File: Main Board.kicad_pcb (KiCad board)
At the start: 2 copper layers, 268 parts, among them J1 Motor Y, J10 CA58SUB-B, J11 PC6 EPSON MAINBOARD, J12 WASTE INK, J13 LED 1, J14 LED 2, J15 Y AXIS, J16 Z AXIS, J17 Power Input, J18 TABLE SENSOR, J19 PHOTO SENSOR EMITER, J2 Motor Z, J20 PHOTO SENSOR RECEIVER, J21 EMERGENCY, J22 EPSON POWER IN, J23 EPSON BOARD POWER, J24 Display, J25 SPI Interface, J26 I2C Interface, J27 LED3, J28 LED4, J29 Key 3, J3 USB_B, J30 Key 4, J31 Key 1, J32 Key 2, J4 SWD, J5 DEBUG, J6 LIMIT Z UP, J7 LIMIT Z DOWN, J8 LIMIT Y BACK, J9 LIMIT Y FRONT, K1 S13-24V-2C, Q1 BC817, Q2 BC817, Q3 BC817, Q4 YJS9435A, Q5 BC817, Q6 BC817, Q7 BC817, Q8 BC817, Q9 BC817, U1 TMC2209-LA, U10 SHTC3, U2 TMC2209-LA, U3 STM32F401VETx, U4 USBUF02W6, U5 74HC245, U6 A4403, U7 MCP16301, U8 74HC2G32, U9 74HC245, Y1 8MHz

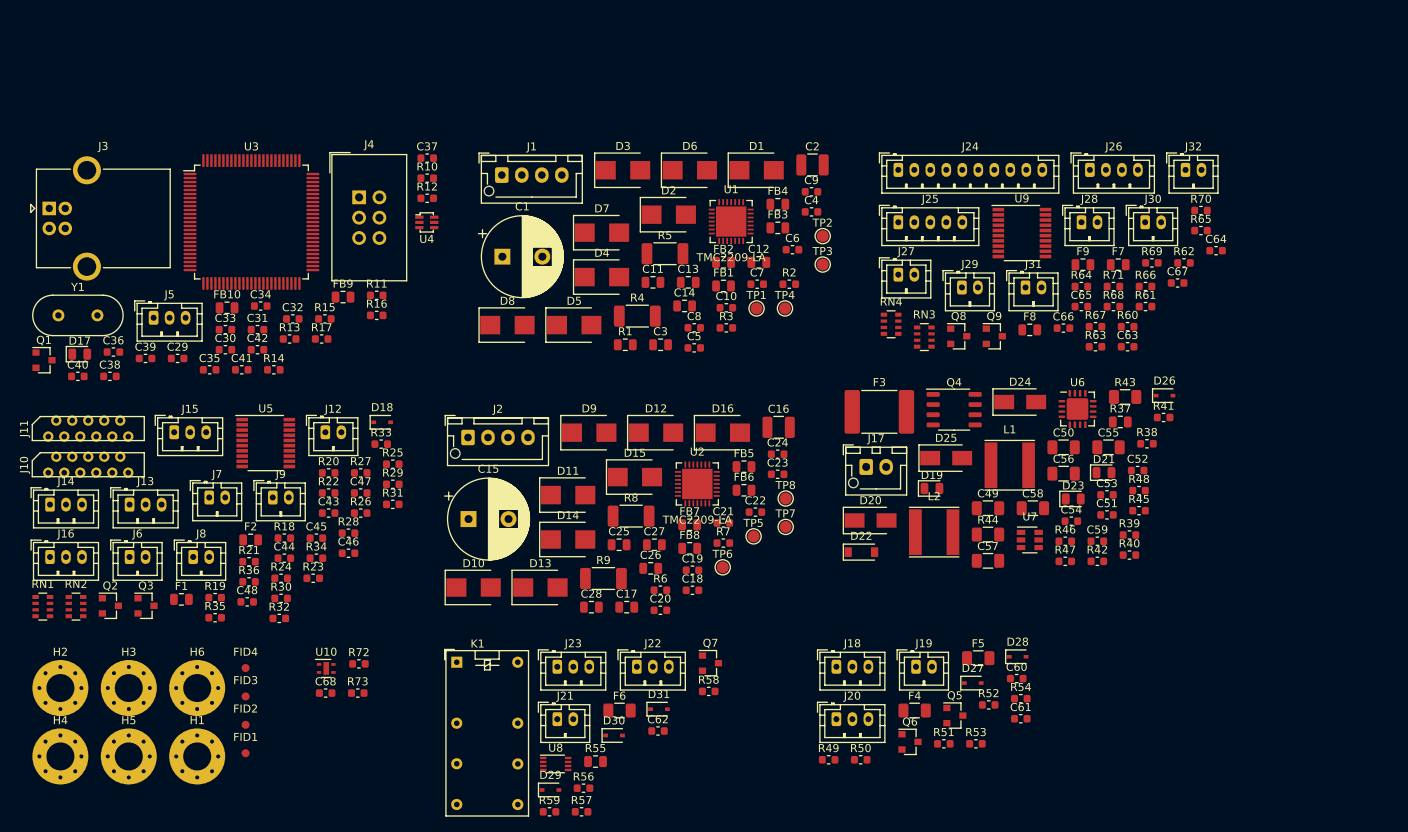
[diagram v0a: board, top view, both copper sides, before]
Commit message: Added 12V regulator, aditional input, outputs, improved inputs ESD
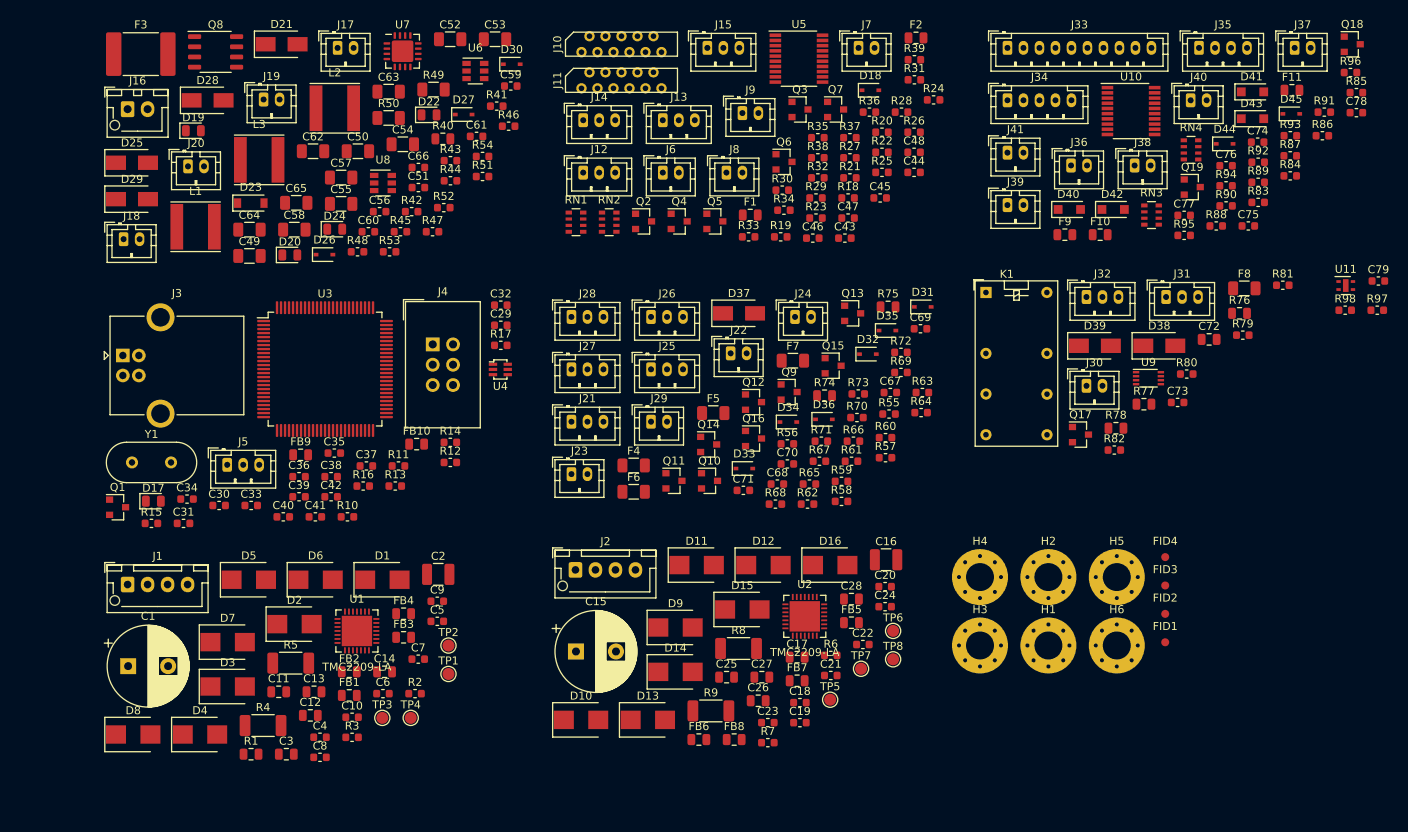
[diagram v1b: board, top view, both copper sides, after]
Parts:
- added C69: 1nF, Capacitor_SMD:C_0603_1608Metric, F.Cu at (137.9, -56.3)
- added C70: 1nF, Capacitor_SMD:C_0603_1608Metric, F.Cu at (121.2, -39.4)
- added C71: 1nF, Capacitor_SMD:C_0603_1608Metric, F.Cu at (115.7, -36.1)
- added C72: NI, Capacitor_SMD:C_0805_2012Metric, F.Cu at (174.0, -54.9)
- added C73: 1nF, Capacitor_SMD:C_0603_1608Metric, F.Cu at (170.0, -47.1)
- added C74: 0.1uF, Capacitor_SMD:C_0603_1608Metric, F.Cu at (180.0, -79.6)
- added C75: 1nF, Capacitor_SMD:C_0603_1608Metric, F.Cu at (178.9, -69.1)
- added C76: 1nF, Capacitor_SMD:C_0603_1608Metric, F.Cu at (176.1, -76.6)
- added C77: 1nF, Capacitor_SMD:C_0603_1608Metric, F.Cu at (170.8, -70.4)
- added C78: 1nF, Capacitor_SMD:C_0603_1608Metric, F.Cu at (192.4, -83.3)
- added C79: 0.1uF, Capacitor_SMD:C_0603_1608Metric, F.Cu at (195.1, -62.2)
- added D32: 1N4448WS-7-F, Diode_SMD:D_SOD-323, F.Cu at (131.3, -53.1)
- added D33: 1N4448WS-7-F, Diode_SMD:D_SOD-323, F.Cu at (115.9, -38.8)
- added D34: SD05C.TCT, Diode_SMD:D_SOD-323, F.Cu at (121.4, -44.6)
- added D35: SD05C.TCT, Diode_SMD:D_SOD-323, F.Cu at (133.8, -56.0)
- added D36: SD05C.TCT, Diode_SMD:D_SOD-323, F.Cu at (125.8, -44.9)
- added D37: B130-13-F, Diode_SMD:D_SMA, F.Cu at (115.2, -58.2)
- added D38: B130-13-F, Diode_SMD:D_SMA, F.Cu at (167.7, -54.1)
- added D39: B130-13-F, Diode_SMD:D_SMA, F.Cu at (159.7, -54.1)
- added D40: SKL32, Diode_SMD:D_SOD-123F, F.Cu at (156.5, -71.2)
- added D41: SKL32, Diode_SMD:D_SOD-123F, F.Cu at (179.4, -85.9)
- added D42: SKL32, Diode_SMD:D_SOD-123F, F.Cu at (162.0, -71.2)
- added D43: SKL32, Diode_SMD:D_SOD-123F, F.Cu at (179.4, -82.5)
- added D44: SD05C.TCT, Diode_SMD:D_SOD-323, F.Cu at (175.9, -79.4)
- added D45: SD05C.TCT, Diode_SMD:D_SOD-323, F.Cu at (184.2, -83.1)
- added F10: SR050, Fuse:Fuse_0805_2012Metric, F.Cu at (160.3, -68.0)
- added F11: SR010, Fuse:Fuse_0805_2012Metric, F.Cu at (184.3, -86.1)
- added J33: Display, Connector_JST:JST_PH_B10B-PH-K_1x10_P2.00mm_Vertical, F.Cu at (148.8, -91.4)
- added J34: SPI Interface, Connector_JST:JST_PH_B5B-PH-K_1x05_P2.00mm_Vertical, F.Cu at (148.8, -84.8)
- added J35: I2C Interface, Connector_JST:JST_PH_B4B-PH-K_1x04_P2.00mm_Vertical, F.Cu at (172.7, -91.4)
- added J36: LED4, Connector_JST:JST_PH_B2B-PH-K_1x02_P2.00mm_Vertical, F.Cu at (156.7, -76.7)
- added J37: LED3, Connector_JST:JST_PH_B2B-PH-K_1x02_P2.00mm_Vertical, F.Cu at (184.7, -91.4)
- added J38: Key 3, Connector_JST:JST_PH_B2B-PH-K_1x02_P2.00mm_Vertical, F.Cu at (164.7, -76.7)
- added J39: Key 4, Connector_JST:JST_PH_B2B-PH-K_1x02_P2.00mm_Vertical, F.Cu at (148.8, -71.7)
- added J40: Key 1, Connector_JST:JST_PH_B2B-PH-K_1x02_P2.00mm_Vertical, F.Cu at (171.7, -84.8)
- added J41: Key 2, Connector_JST:JST_PH_B2B-PH-K_1x02_P2.00mm_Vertical, F.Cu at (148.8, -78.3)
- added L3: DJNR6045-6R8, footprints:L_6.2x6.2_H4.5, F.Cu at (55.2, -77.4)
- added Q10: 2N7002K, Package_TO_SOT_SMD:SOT-23, F.Cu at (111.5, -37.3)
- added Q11: BC817, Package_TO_SOT_SMD:SOT-23, F.Cu at (107.1, -37.3)
- added Q12: BC817, Package_TO_SOT_SMD:SOT-23, F.Cu at (117.0, -47.1)
- added Q13: BC817, Package_TO_SOT_SMD:SOT-23, F.Cu at (129.4, -58.2)
- added Q14: 2N7002K, Package_TO_SOT_SMD:SOT-23, F.Cu at (111.4, -41.8)
- added Q15: 2N7002K, Package_TO_SOT_SMD:SOT-23, F.Cu at (127.0, -51.6)
- added Q16: 2N7002K, Package_TO_SOT_SMD:SOT-23, F.Cu at (117.0, -42.5)
- added Q17: BC817, Package_TO_SOT_SMD:SOT-23, F.Cu at (157.9, -43.0)
- added Q18: 2N7002K, Package_TO_SOT_SMD:SOT-23, F.Cu at (191.9, -91.8)
- added Q19: 2N7002K, Package_TO_SOT_SMD:SOT-23, F.Cu at (171.9, -74.0)
- added R74: NI, Resistor_SMD:R_0805_2012Metric, F.Cu at (125.9, -47.9)
- added R75: NI, Resistor_SMD:R_0805_2012Metric, F.Cu at (133.8, -59.0)
- added R76: 0Ω, Resistor_SMD:R_0805_2012Metric, F.Cu at (177.8, -58.2)
- added R77: NI, Resistor_SMD:R_0805_2012Metric, F.Cu at (165.8, -46.8)
- added R78: NI, Resistor_SMD:R_0805_2012Metric, F.Cu at (162.3, -43.8)
- added R79: 100kΩ, Resistor_SMD:R_0603_1608Metric, F.Cu at (178.2, -55.5)
- added R80: 1kΩ, Resistor_SMD:R_0603_1608Metric, F.Cu at (171.2, -50.6)
- added R81: 100kΩ, Resistor_SMD:R_0603_1608Metric, F.Cu at (183.2, -61.7)
- added R82: 100kΩ, Resistor_SMD:R_0603_1608Metric, F.Cu at (162.1, -41.1)
- added R83: 20Ω, Resistor_SMD:R_0603_1608Metric, F.Cu at (180.1, -72.1)
- added R84: 20Ω, Resistor_SMD:R_0603_1608Metric, F.Cu at (184.1, -75.4)
- added R85: 100Ω, Resistor_SMD:R_0603_1608Metric, F.Cu at (192.4, -85.8)
- added R86: 100Ω, Resistor_SMD:R_0603_1608Metric, F.Cu at (188.1, -80.4)
- added R87: 330Ω, Resistor_SMD:R_0603_1608Metric, F.Cu at (184.1, -77.9)
- added R88: 330Ω, Resistor_SMD:R_0603_1608Metric, F.Cu at (174.9, -69.1)
- added R89: 4.7kΩ, Resistor_SMD:R_0603_1608Metric, F.Cu at (180.1, -74.6)
- added R90: 4.7kΩ, Resistor_SMD:R_0603_1608Metric, F.Cu at (176.1, -71.6)
- added R91: 4.7kΩ, Resistor_SMD:R_0603_1608Metric, F.Cu at (188.4, -83.3)
- added R92: 4.7kΩ, Resistor_SMD:R_0603_1608Metric, F.Cu at (180.1, -77.1)
- added R93: 1kΩ, Resistor_SMD:R_0603_1608Metric, F.Cu at (184.1, -80.4)
- added R94: 1kΩ, Resistor_SMD:R_0603_1608Metric, F.Cu at (176.1, -74.1)
- added R95: 1kΩ, Resistor_SMD:R_0603_1608Metric, F.Cu at (170.8, -67.9)
- added R96: 1kΩ, Resistor_SMD:R_0603_1608Metric, F.Cu at (191.6, -88.3)
- added R97: 2.2kΩ, Resistor_SMD:R_0603_1608Metric, F.Cu at (195.0, -58.6)
- added R98: 2.2kΩ, Resistor_SMD:R_0603_1608Metric, F.Cu at (191.0, -58.6)
- added U11: SHTC3, footprints:DFN-4-1EP_2x2mm_P1mm_EP0.7x1.6mm, F.Cu at (191.0, -61.7)
- C47, C61: value 1nF -> 0.1uF
- C48, C68: value 0.1uF -> 1nF
- C51: value 47nF -> 0.1uF
- C52: value 22nF -> 2.2uF; footprint Capacitor_SMD:C_0603_1608Metric -> Capacitor_SMD:C_1206_3216Metric
- C53: value 1nF -> 2.2uF; footprint Capacitor_SMD:C_0603_1608Metric -> Capacitor_SMD:C_1206_3216Metric
- C54: value 0.1uF -> 2.2uF; footprint Capacitor_SMD:C_0603_1608Metric -> Capacitor_SMD:C_1206_3216Metric
- C55: value 10uF -> 2.2uF
- C56: value 10uF -> 47nF; footprint Capacitor_SMD:C_1206_3216Metric -> Capacitor_SMD:C_0603_1608Metric
- C59: value 10nF -> 22nF
- C62, C64, C65: value 1nF -> 10uF; footprint Capacitor_SMD:C_0603_1608Metric -> Capacitor_SMD:C_1206_3216Metric
- C63: value 0.1uF -> 10uF; footprint Capacitor_SMD:C_0603_1608Metric -> Capacitor_SMD:C_1206_3216Metric
- C66: value 1nF -> 10nF
- D18: value 1N4448WS-7-F -> SD05C.TCT
- D20: value P4SMA30CA -> OF-SMD2012G-1; footprint Diode_SMD:D_SMA -> Diode_SMD:D_0805_2012Metric
- D21: value OF-SMD2012G-1 -> P4SMA30CA; footprint Diode_SMD:D_0805_2012Metric -> Diode_SMD:D_SMA
- D22: value MMSZ5240B-7-F -> OF-SMD2012G-1; footprint Diode_SMD:D_SOD-123 -> Diode_SMD:D_0805_2012Metric
- D23: value OF-SMD2012G-1 -> MMSZ5240B-7-F; footprint Diode_SMD:D_0805_2012Metric -> Diode_SMD:D_SOD-123
- D24: value B140-13-F -> OF-SMD2012G-1; footprint Diode_SMD:D_SMA -> Diode_SMD:D_0805_2012Metric
- D25: value SK35SMA -> B140-13-F
- D27: value 1N4448WS-7-F -> MMSZ5236BS-7-F
- D28: value 1N4448WS-7-F -> B140-13-F; footprint Diode_SMD:D_SOD-323 -> Diode_SMD:D_SMA
- D29: value 1N4448WS-7-F -> SK35SMA; footprint Diode_SMD:D_SOD-323 -> Diode_SMD:D_SMA
- F7: value SR010 -> Polyfuse; footprint Fuse:Fuse_0805_2012Metric -> Fuse:Fuse_1206_3216Metric
- F8: value SR050 -> SN010-60; footprint Fuse:Fuse_0805_2012Metric -> Fuse:Fuse_1206_3216Metric
- J12: value WASTE INK -> Y AXIS; footprint Connector_JST:JST_PH_B2B-PH-K_1x02_P2.00mm_Vertical -> Connector_JST:JST_PH_B3B-PH-K_1x03_P2.00mm_Vertical
- J13: value LED 1 -> Z AXIS
- J14: value LED 2 -> LED 1
- J15: value Y AXIS -> LED 2
- J16: value Z AXIS -> Power Input; footprint Connector_JST:JST_PH_B3B-PH-K_1x03_P2.00mm_Vertical -> Connector_JST:JST_XH_B2B-XH-AM_1x02_P2.50mm_Vertical
- J17: value Power Input -> VS; footprint Connector_JST:JST_XH_B2B-XH-AM_1x02_P2.50mm_Vertical -> Connector_JST:JST_PH_B2B-PH-K_1x02_P2.00mm_Vertical
- J18: value TABLE SENSOR -> 12V; footprint Connector_JST:JST_PH_B3B-PH-K_1x03_P2.00mm_Vertical -> Connector_JST:JST_PH_B2B-PH-K_1x02_P2.00mm_Vertical
- J19: value PHOTO SENSOR EMITER -> 5V
- J20: value PHOTO SENSOR RECEIVER -> 3.3V; footprint Connector_JST:JST_PH_B3B-PH-K_1x03_P2.00mm_Vertical -> Connector_JST:JST_PH_B2B-PH-K_1x02_P2.00mm_Vertical
- J21: value EMERGENCY -> TABLE SENSOR; footprint Connector_JST:JST_PH_B2B-PH-K_1x02_P2.00mm_Vertical -> Connector_JST:JST_PH_B3B-PH-K_1x03_P2.00mm_Vertical
- J22: value EPSON POWER IN -> INPUT1; footprint Connector_JST:JST_PH_B3B-PH-K_1x03_P2.00mm_Vertical -> Connector_JST:JST_PH_B2B-PH-K_1x02_P2.00mm_Vertical
- J23: value EPSON BOARD POWER -> INPUT2; footprint Connector_JST:JST_PH_B3B-PH-K_1x03_P2.00mm_Vertical -> Connector_JST:JST_PH_B2B-PH-K_1x02_P2.00mm_Vertical
- J24: value Display -> PHOTO SENSOR EMITER; footprint Connector_JST:JST_PH_B10B-PH-K_1x10_P2.00mm_Vertical -> Connector_JST:JST_PH_B2B-PH-K_1x02_P2.00mm_Vertical
- J25: value SPI Interface -> PHOTO SENSOR RECEIVER; footprint Connector_JST:JST_PH_B5B-PH-K_1x05_P2.00mm_Vertical -> Connector_JST:JST_PH_B3B-PH-K_1x03_P2.00mm_Vertical
- J26: value I2C Interface -> INPUT3; footprint Connector_JST:JST_PH_B4B-PH-K_1x04_P2.00mm_Vertical -> Connector_JST:JST_PH_B3B-PH-K_1x03_P2.00mm_Vertical
- J27: value LED3 -> OUT1; footprint Connector_JST:JST_PH_B2B-PH-K_1x02_P2.00mm_Vertical -> Connector_JST:JST_PH_B3B-PH-K_1x03_P2.00mm_Vertical
- J28: value LED4 -> OUT2; footprint Connector_JST:JST_PH_B2B-PH-K_1x02_P2.00mm_Vertical -> Connector_JST:JST_PH_B3B-PH-K_1x03_P2.00mm_Vertical
- J29: value Key 3 -> RELAY
- J30: value Key 4 -> EMERGENCY
- J31: value Key 1 -> EPSON POWER IN; footprint Connector_JST:JST_PH_B2B-PH-K_1x02_P2.00mm_Vertical -> Connector_JST:JST_PH_B3B-PH-K_1x03_P2.00mm_Vertical
- J32: value Key 2 -> EPSON BOARD POWER; footprint Connector_JST:JST_PH_B2B-PH-K_1x02_P2.00mm_Vertical -> Connector_JST:JST_PH_B3B-PH-K_1x03_P2.00mm_Vertical
- J6: value LIMIT Z UP -> LIMIT Y BACK
- J7: value LIMIT Z DOWN -> LIMIT Y FRONT
- J8: value LIMIT Y BACK -> LIMIT Z UP
- J9: value LIMIT Y FRONT -> LIMIT Z DOWN
- L1: value DJNR6045-150 -> DJNR6045-680
- L2: value DJNR6045-6R8 -> DJNR6045-150
- Q2, Q3, Q5, Q6, Q7, Q9: value BC817 -> 2N7002K
- Q4: value YJS9435A -> 2N7002K; footprint Package_SO:SOP-8_3.9x4.9mm_P1.27mm -> Package_TO_SOT_SMD:SOT-23
- Q8: value BC817 -> YJS9435A; footprint Package_TO_SOT_SMD:SOT-23 -> Package_SO:SOP-8_3.9x4.9mm_P1.27mm
- R22, R23, R24, R25, R30, R71: value 1kΩ -> 100Ω
- R26, R27: value 0Ω -> 47kΩ
- R28: value NI -> 47kΩ
- R29, R70: value 1kΩ -> 47kΩ
- R31: value 4.7kΩ -> 1kΩ
- R32: value 1kΩ -> 0Ω
- R33: value 4.7kΩ -> 0Ω
- R34: value 10kΩ -> NI
- R35, R60, R61: value 4.7kΩ -> 100Ω
- R36, R69: value 1kΩ -> 100kΩ
- R37: value 10kΩ -> 47kΩ; footprint Resistor_SMD:R_0805_2012Metric -> Resistor_SMD:R_0603_1608Metric
- R38: value 330Ω -> 1kΩ
- R39: value 100kΩ -> 1kΩ
- R40: value 1kΩ -> 10kΩ; footprint Resistor_SMD:R_0603_1608Metric -> Resistor_SMD:R_0805_2012Metric
- R41: value 100kΩ -> 330Ω
- R42: value 47Ω -> 1kΩ
- R43: value 100mΩ -> 100kΩ; footprint Resistor_SMD:R_1206_3216Metric -> Resistor_SMD:R_0603_1608Metric
- R44: value 100mΩ -> 2.7kΩ; footprint Resistor_SMD:R_1206_3216Metric -> Resistor_SMD:R_0603_1608Metric
- R45: value 31.2kΩ -> 140kΩ
- R47: value 3.92kΩ -> 100kΩ
- R48: value 750Ω -> 47Ω
- R49, R50: value 10kΩ -> 100mΩ; footprint Resistor_SMD:R_0603_1608Metric -> Resistor_SMD:R_1206_3216Metric
- R51: value 33kΩ -> 31.2kΩ
- R52: value 33kΩ -> 10kΩ
- R53: value 10kΩ -> 3.92kΩ
- R54: value 10kΩ -> 750Ω
- R55: value 1kΩ -> 10kΩ; footprint Resistor_SMD:R_0805_2012Metric -> Resistor_SMD:R_0603_1608Metric
- R56: value 33kΩ -> 4.7kΩ
- R57: value 1kΩ -> 4.7kΩ
- R58: value 100kΩ -> 10kΩ
- R62: value 330Ω -> 100kΩ
- R63: value 330Ω -> 47kΩ
- R64, R65, R66: value 4.7kΩ -> 47kΩ
- R67: value 4.7kΩ -> 10kΩ
- R68: value 1kΩ -> NI
- R72, R73: value 2.2kΩ -> 100Ω
- U10: value SHTC3 -> 74HC245; footprint footprints:DFN-4-1EP_2x2mm_P1mm_EP0.7x1.6mm -> Package_SO:TSSOP-20_4.4x6.5mm_P0.65mm
- U6: value A4403 -> MCP16301; footprint Package_DFN_QFN:QFN-16-1EP_4x4mm_P0.65mm_EP2.7x2.7mm -> Package_TO_SOT_SMD:SOT-23-6
- U7: value MCP16301 -> A4403; footprint Package_TO_SOT_SMD:SOT-23-6 -> Package_DFN_QFN:QFN-16-1EP_4x4mm_P0.65mm_EP2.7x2.7mm
- U8: value 74HC2G32 -> MCP16301; footprint Package_SO:VSSOP-8_2.3x2mm_P0.5mm -> Package_TO_SOT_SMD:SOT-23-6
- U9: value 74HC245 -> 74HC2G32; footprint Package_SO:TSSOP-20_4.4x6.5mm_P0.65mm -> Package_SO:VSSOP-8_2.3x2mm_P0.5mm
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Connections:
- net Net-(J3-Pad2) renamed /Microcontroller/D-
- net Net-(J3-Pad3) renamed /Microcontroller/D+
- C43 pad 1: LIMIT_Z_UP -> LIMIT_Y_BACK
- C44 pad 1: LIMIT_Z_DOWN -> LIMIT_Y_FRONT
- C45 pad 1: LIMIT_Y_BACK -> LIMIT_Z_UP
- C46 pad 1: LIMIT_Y_FRONT -> LIMIT_Z_DOWN
- C47 pad 1: WASTE_INK -> +5V
- C48 pad 1: +5V -> PRINTER_POWER_DETECT
- C51 pad 1: GND -> Net-(C51-Pad1)
- C52 pad 1: Net-(C52-Pad1) -> VS
- C52 pad 2: Net-(C52-Pad2) -> GND
- C53 pad 1: Net-(C53-Pad1) -> VS
- C54 pad 1: Net-(C54-Pad1) -> VS
- C54 pad 2: Net-(C54-Pad2) -> GND
- C55 pad 1: +5V -> VS
- C56 pad 1: +3V3 -> GND
- C56 pad 2: GND -> Net-(C56-Pad2)
- C57 pad 1: +5V -> +12V
- C58 pad 1: +3V3 -> +12V
- C59 pad 1: +5V -> Net-(C59-Pad1)
- C60 pad 1: TABLE_SENSOR -> Net-(C60-Pad1)
- C61 pad 1: PHOTO_SENSOR -> Net-(C61-Pad1)
- C61 pad 2: GND -> Net-(C61-Pad2)
- C62 pad 1: EMERGENCY -> +5V
- C63 pad 1: +5V -> +3V3
- C64 pad 1: KEY_3 -> +5V
- C65 pad 1: KEY_4 -> +3V3
- C66 pad 1: KEY_1 -> +5V
- C66 pad 2: GND -> Net-(C66-Pad2)
- C67 pad 1: KEY_2 -> INPUT1
- C68 pad 1: +3V3 -> INPUT2
- D18 pad 1: Net-(D18-Pad1) -> /Sockets/OPE
- D22 pad 1: VS -> GND
- D23 pad 1: GND -> VS
- D24 pad 1: Net-(C54-Pad2) -> GND
- D24 pad 2: GND -> Net-(D24-Pad2)
- D25 pad 1: Net-(C52-Pad2) -> Net-(C51-Pad2)
- D25 pad 2: Net-(D25-Pad2) -> GND
- D26 pad 1: Net-(C54-Pad1) -> Net-(C51-Pad1)
- D26 pad 2: +3V3 -> Net-(D26-Pad2)
- D27 pad 1: Net-(D27-Pad1) -> +12V
- D27 pad 2: GND -> Net-(D26-Pad2)
- D28 pad 1: Net-(D28-Pad1) -> Net-(C61-Pad2)
- D29 pad 1: Net-(D29-Pad1) -> Net-(C59-Pad2)
- D29 pad 2: GND -> Net-(D29-Pad2)
- D30 pad 1: VS -> Net-(C61-Pad1)
- D30 pad 2: Net-(D30-Pad2) -> +3V3
- D31 pad 1: Net-(D30-Pad2) -> Net-(D31-Pad1)
- F3 pad 1: Net-(D20-Pad2) -> Net-(D21-Pad2)
- F6 pad 1: Net-(F6-Pad1) -> VS
- F6 pad 2: VS -> Net-(F6-Pad2)
- F7 pad 1: +5V -> Net-(D37-Pad1)
- F7 pad 2: Net-(F7-Pad2) -> +12V
- F8 pad 1: +5V -> Net-(F8-Pad1)
- F8 pad 2: Net-(F8-Pad2) -> VS
- F9 pad 1: +3V3 -> +5V
- J12 pad 1: Net-(J12-Pad1) -> /Sockets/YSTEP
- J13 pad 1: Net-(F1-Pad2) -> /Sockets/ZSTEP
- J13 pad 2: /Sockets/LED1_CNT -> GND
- J13 pad 3: GND -> /Sockets/ZDIR
- J14 pad 1: Net-(F2-Pad2) -> Net-(F1-Pad2)
- J14 pad 2: /Sockets/LED2_CNT -> /Sockets/LED1_CNT
- J15 pad 1: /Sockets/YSTEP -> Net-(F2-Pad2)
- J15 pad 2: GND -> /Sockets/LED2_CNT
- J15 pad 3: /Sockets/YDIR -> GND
- J16 pad 1: /Sockets/ZSTEP -> Net-(F3-Pad2)
- J17 pad 1: Net-(F3-Pad2) -> VS
- J18 pad 1: Net-(F4-Pad2) -> +12V
- J18 pad 2: Net-(J18-Pad2) -> GND
- J19 pad 1: Net-(F5-Pad2) -> +5V
- J20 pad 1: Net-(F5-Pad2) -> +3V3
- J20 pad 2: Net-(J20-Pad2) -> GND
- J21 pad 1: Net-(F6-Pad1) -> Net-(F4-Pad2)
- J21 pad 2: Net-(D29-Pad1) -> Net-(J21-Pad2)
- J22 pad 2: Net-(J22-Pad2) -> GND
- J23 pad 2: Net-(J22-Pad2) -> GND
- J24 pad 1: Net-(F7-Pad2) -> Net-(F5-Pad2)
- J24 pad 2: Net-(J24-Pad2) -> GND
- J25 pad 1: Net-(F8-Pad2) -> Net-(F5-Pad2)
- J25 pad 2: SPI_MOSI_BUF -> Net-(J25-Pad2)
- J25 pad 3: SPI_SCLK_BUF -> GND
- J26 pad 1: Net-(F9-Pad2) -> Net-(F6-Pad2)
- J26 pad 2: I2C_SDA -> Net-(J26-Pad2)
- J27 pad 2: Net-(J27-Pad2) -> Net-(D34-Pad1)
- J28 pad 2: Net-(J28-Pad2) -> Net-(D35-Pad1)
- J29 pad 1: Net-(J29-Pad1) -> Net-(D36-Pad1)
- J29 pad 2: GND -> Net-(D37-Pad1)
- J30 pad 1: Net-(J30-Pad1) -> Net-(F8-Pad1)
- J30 pad 2: GND -> Net-(D38-Pad1)
- J31 pad 2: GND -> Net-(C72-Pad2)
- J32 pad 2: GND -> Net-(C72-Pad2)
- K1 pad 1: Net-(D29-Pad1) -> Net-(D38-Pad1)
- K1 pad 13: Net-(J22-Pad3) -> Net-(K1-Pad13)
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
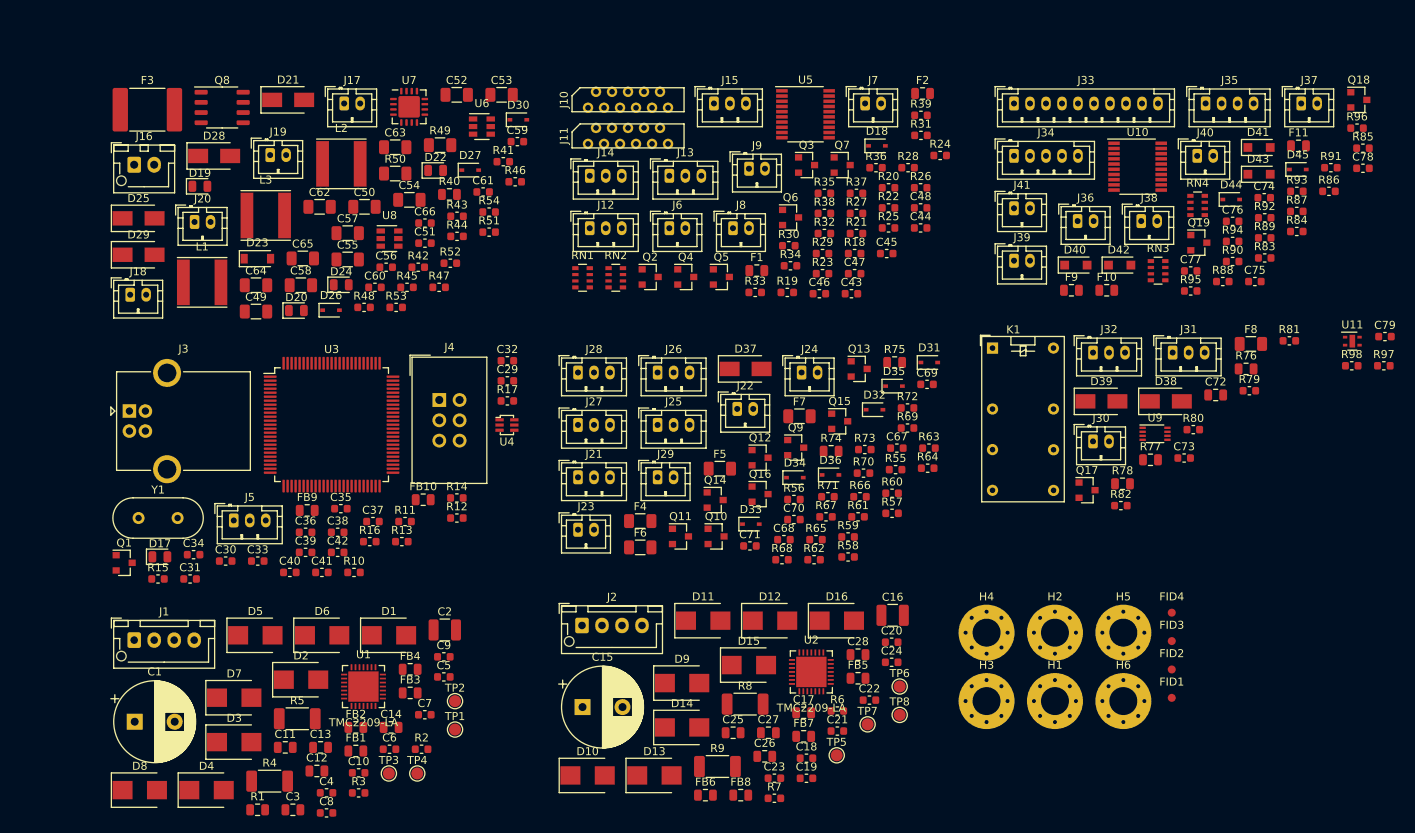
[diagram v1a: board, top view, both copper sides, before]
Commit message: Added analog input
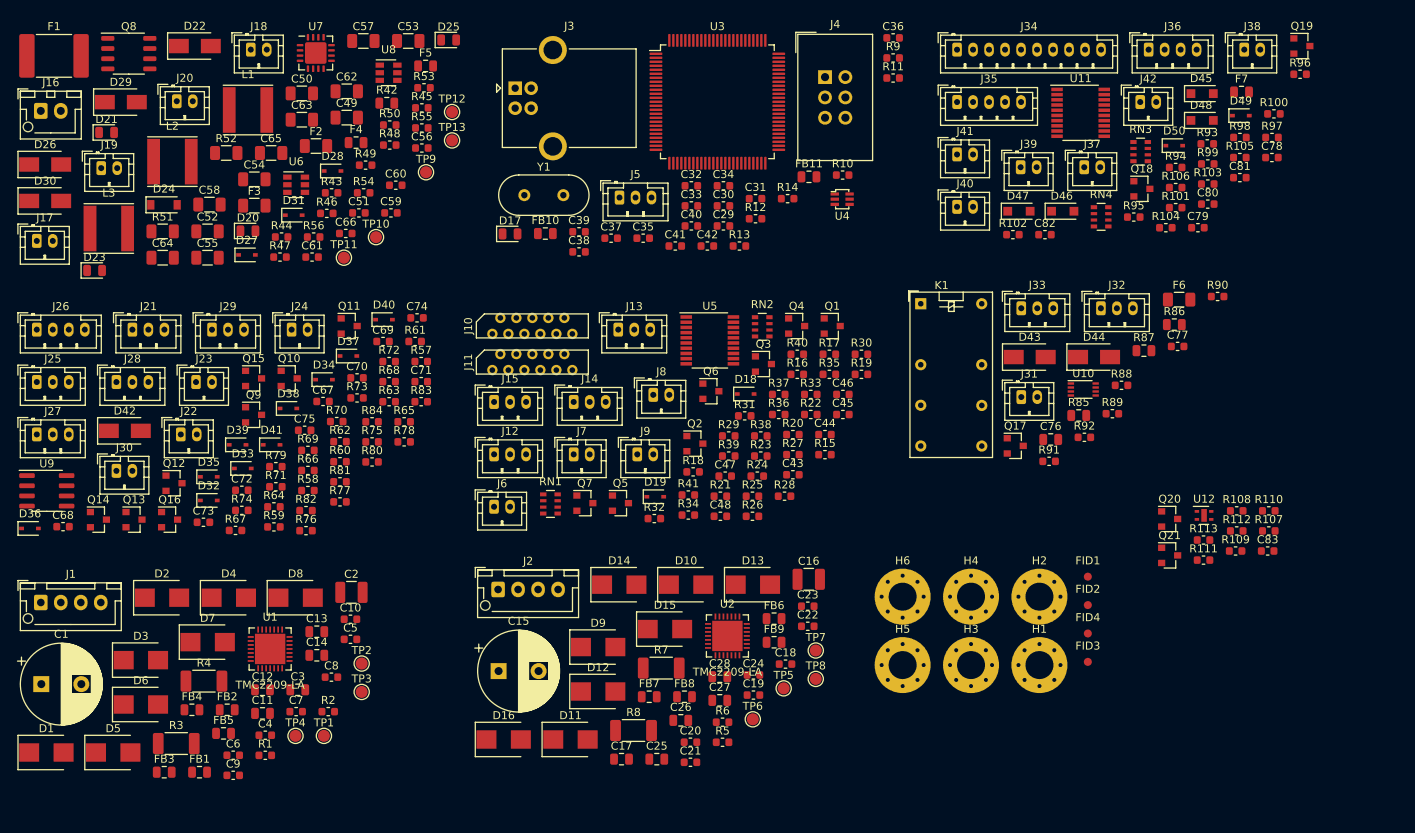
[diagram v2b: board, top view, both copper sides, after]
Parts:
- removed F10: SR050, Fuse:Fuse_0805_2012Metric
- removed F11, F9: SR010, Fuse:Fuse_0805_2012Metric
- removed F8: SN010-60, Fuse:Fuse_1206_3216Metric
- added C80: 1nF, Capacitor_SMD:C_0603_1608Metric, F.Cu at (173.0, -78.8)
- added C81: 1nF, Capacitor_SMD:C_0603_1608Metric, F.Cu at (177.0, -82.1)
- added C82: 1nF, Capacitor_SMD:C_0603_1608Metric, F.Cu at (152.6, -75.0)
- added C83: 0.1uF, Capacitor_SMD:C_0603_1608Metric, F.Cu at (180.5, -35.4)
- added D46: SKL32, Diode_SMD:D_SOD-123F, F.Cu at (154.9, -77.9)
- added D47: SKL32, Diode_SMD:D_SOD-123F, F.Cu at (149.4, -77.9)
- added D48: SKL32, Diode_SMD:D_SOD-123F, F.Cu at (172.3, -89.3)
- added D49: SD05C.TCT, Diode_SMD:D_SOD-323, F.Cu at (177.1, -89.9)
- added D50: SD05C.TCT, Diode_SMD:D_SOD-323, F.Cu at (168.8, -86.1)
- added FB11: 1000@100MHz, Inductor_SMD:L_0805_2012Metric, F.Cu at (123.1, -82.2)
- added J42: Key 2, Connector_JST:JST_PH_B2B-PH-K_1x02_P2.00mm_Vertical, F.Cu at (164.5, -91.6)
- added Q20: 2N7002K, Package_TO_SOT_SMD:SOT-23, F.Cu at (168.2, -39.4)
- added Q21: 2N7002K, Package_TO_SOT_SMD:SOT-23, F.Cu at (168.2, -34.9)
- added R100: 4.7kΩ, Resistor_SMD:R_0603_1608Metric, F.Cu at (181.2, -90.1)
- added R101: 4.7kΩ, Resistor_SMD:R_0603_1608Metric, F.Cu at (169.0, -78.4)
- added R102: 4.7kΩ, Resistor_SMD:R_0603_1608Metric, F.Cu at (148.6, -75.0)
- added R103: 1kΩ, Resistor_SMD:R_0603_1608Metric, F.Cu at (173.0, -81.3)
- added R104: 1kΩ, Resistor_SMD:R_0603_1608Metric, F.Cu at (167.7, -75.8)
- added R105: 1kΩ, Resistor_SMD:R_0603_1608Metric, F.Cu at (177.0, -84.6)
- added R106: 1kΩ, Resistor_SMD:R_0603_1608Metric, F.Cu at (169.0, -80.9)
- added R107: 2.2kΩ, Resistor_SMD:R_0603_1608Metric, F.Cu at (180.6, -37.9)
- added R108: 0Ω, Resistor_SMD:R_0603_1608Metric, F.Cu at (176.6, -40.5)
- added R109: 2.2kΩ, Resistor_SMD:R_0603_1608Metric, F.Cu at (176.5, -35.4)
- added R110: 100Ω, Resistor_SMD:R_0603_1608Metric, F.Cu at (180.6, -40.5)
- added R111: 100Ω, Resistor_SMD:R_0603_1608Metric, F.Cu at (172.4, -34.3)
- added R112: 47kΩ, Resistor_SMD:R_0603_1608Metric, F.Cu at (176.6, -37.9)
- added R113: 47kΩ, Resistor_SMD:R_0603_1608Metric, F.Cu at (172.4, -36.8)
- added R99: 4.7kΩ, Resistor_SMD:R_0603_1608Metric, F.Cu at (173.0, -83.8)
- added TP10: 5V, TestPoint:TestPoint_Pad_D1.5mm, F.Cu at (69.0, -74.7)
- added TP11: 3.3V, TestPoint:TestPoint_Pad_D1.5mm, F.Cu at (65.0, -72.1)
- added TP12: 12V, TestPoint:TestPoint_Pad_D1.5mm, F.Cu at (78.5, -90.3)
- added TP13: GND, TestPoint:TestPoint_Pad_D1.5mm, F.Cu at (78.5, -86.8)
- added TP9: VS, TestPoint:TestPoint_Pad_D1.5mm, F.Cu at (75.3, -82.8)
- added U12: SHTC3, footprints:DFN-4-1EP_2x2mm_P1mm_EP0.7x1.6mm, F.Cu at (172.5, -39.9)
- C71, C73: value 1nF -> NI
- C72: footprint Capacitor_SMD:C_0805_2012Metric -> Capacitor_SMD:C_0603_1608Metric
- C74: value 0.1uF -> NI
- C76: value 1nF -> NI; footprint Capacitor_SMD:C_0603_1608Metric -> Capacitor_SMD:C_0805_2012Metric
- C78: value 1nF -> 0.1uF
- C79: value 0.1uF -> 1nF
- D19: value OF-SMD2012G-1 -> SD05C.TCT; footprint Diode_SMD:D_0805_2012Metric -> Diode_SMD:D_SOD-323
- D21: value P4SMA30CA -> OF-SMD2012G-1; footprint Diode_SMD:D_SMA -> Diode_SMD:D_0805_2012Metric
- D22: value OF-SMD2012G-1 -> P4SMA30CA; footprint Diode_SMD:D_0805_2012Metric -> Diode_SMD:D_SMA
- D23: value MMSZ5240B-7-F -> OF-SMD2012G-1; footprint Diode_SMD:D_SOD-123 -> Diode_SMD:D_0805_2012Metric
- D24: value OF-SMD2012G-1 -> MMSZ5240B-7-F; footprint Diode_SMD:D_0805_2012Metric -> Diode_SMD:D_SOD-123
- D25: value B140-13-F -> OF-SMD2012G-1; footprint Diode_SMD:D_SMA -> Diode_SMD:D_0805_2012Metric
- D26: value 1N4448WS-7-F -> B140-13-F; footprint Diode_SMD:D_SOD-323 -> Diode_SMD:D_SMA
- D27: value MMSZ5236BS-7-F -> 1N4448WS-7-F
- D28: value B140-13-F -> MMSZ5236BS-7-F; footprint Diode_SMD:D_SMA -> Diode_SMD:D_SOD-323
- D29: value SK35SMA -> B140-13-F
- D30: value 1N4448WS-7-F -> SK35SMA; footprint Diode_SMD:D_SOD-323 -> Diode_SMD:D_SMA
- D34, D35, D36: value SD05C.TCT -> 1N4448WS-7-F
- D37, D38: value B130-13-F -> 1N4448WS-7-F; footprint Diode_SMD:D_SMA -> Diode_SMD:D_SOD-323
- D39: value B130-13-F -> SD05C.TCT; footprint Diode_SMD:D_SMA -> Diode_SMD:D_SOD-323
- D40, D41: value SKL32 -> SD05C.TCT; footprint Diode_SMD:D_SOD-123F -> Diode_SMD:D_SOD-323
- D42, D43: value SKL32 -> B130-13-F; footprint Diode_SMD:D_SOD-123F -> Diode_SMD:D_SMA
- D44: value SD05C.TCT -> B130-13-F; footprint Diode_SMD:D_SOD-323 -> Diode_SMD:D_SMA
- D45: value SD05C.TCT -> SKL32; footprint Diode_SMD:D_SOD-323 -> Diode_SMD:D_SOD-123F
- F1: value SR050 -> 0ZCF0185FF2C; footprint Fuse:Fuse_0805_2012Metric -> Fuse:Fuse_2920_7451Metric
- F2: value SR050 -> SN010-60; footprint Fuse:Fuse_0805_2012Metric -> Fuse:Fuse_1206_3216Metric
- F3: value 0ZCF0185FF2C -> SN010-60; footprint Fuse:Fuse_2920_7451Metric -> Fuse:Fuse_1206_3216Metric
- F4, F5: value SN010-60 -> SR050; footprint Fuse:Fuse_1206_3216Metric -> Fuse:Fuse_0805_2012Metric
- F7: value Polyfuse -> SR050; footprint Fuse:Fuse_1206_3216Metric -> Fuse:Fuse_0805_2012Metric
- FB1: value 60Ohm@100MHz -> 1000@100MHz
- FB9: value 1000@100MHz -> 60Ohm@100MHz
- J26: value INPUT3 -> ANALOG; footprint Connector_JST:JST_PH_B3B-PH-K_1x03_P2.00mm_Vertical -> Connector_JST:JST_PH_B4B-PH-K_1x04_P2.00mm_Vertical
- J27: value OUT1 -> INPUT3
- J28: value OUT2 -> OUT1
- J29: value RELAY -> OUT2; footprint Connector_JST:JST_PH_B2B-PH-K_1x02_P2.00mm_Vertical -> Connector_JST:JST_PH_B3B-PH-K_1x03_P2.00mm_Vertical
- J30: value EMERGENCY -> RELAY
- J31: value EPSON POWER IN -> EMERGENCY; footprint Connector_JST:JST_PH_B3B-PH-K_1x03_P2.00mm_Vertical -> Connector_JST:JST_PH_B2B-PH-K_1x02_P2.00mm_Vertical
- J32: value EPSON BOARD POWER -> EPSON POWER IN
- J33: value Display -> EPSON BOARD POWER; footprint Connector_JST:JST_PH_B10B-PH-K_1x10_P2.00mm_Vertical -> Connector_JST:JST_PH_B3B-PH-K_1x03_P2.00mm_Vertical
- J34: value SPI Interface -> Display; footprint Connector_JST:JST_PH_B5B-PH-K_1x05_P2.00mm_Vertical -> Connector_JST:JST_PH_B10B-PH-K_1x10_P2.00mm_Vertical
- J35: value I2C Interface -> SPI Interface; footprint Connector_JST:JST_PH_B4B-PH-K_1x04_P2.00mm_Vertical -> Connector_JST:JST_PH_B5B-PH-K_1x05_P2.00mm_Vertical
- J36: value LED4 -> I2C Interface; footprint Connector_JST:JST_PH_B2B-PH-K_1x02_P2.00mm_Vertical -> Connector_JST:JST_PH_B4B-PH-K_1x04_P2.00mm_Vertical
- J37: value LED3 -> LED4
- J38: value Key 3 -> LED3
- J39: value Key 4 -> Key 3
- J40: value Key 1 -> Key 4
- J41: value Key 2 -> Key 1
- Q1: value BC817 -> 2N7002K
- R1: value 0Ω -> 1kΩ; footprint Resistor_SMD:R_0805_2012Metric -> Resistor_SMD:R_0603_1608Metric
- R12: value 47RΩ -> 0Ω
- R13, R14: value 10kΩ -> 330Ω
- R15: value 0Ω -> 4.7kΩ
- R16, R17: value 330Ω -> 4.7kΩ
- R19, R20, R21: value 4.7kΩ -> 100Ω
- R2, R6, R80: value 1kΩ -> 100kΩ
- R23, R24, R25: value 100Ω -> 47kΩ
- R27, R63: value 47kΩ -> 100Ω
- R28: value 47kΩ -> 1kΩ
- R29: value 47kΩ -> 0Ω
- R3, R7: value 100kΩ -> 100mΩ; footprint Resistor_SMD:R_0603_1608Metric -> Resistor_SMD:R_2010_5025Metric
- R30: value 100Ω -> 0Ω
- R31: value 1kΩ -> 0Ω
- R32: value 0Ω -> NI
- R34: value NI -> 0Ω
- R38, R95, R96: value 1kΩ -> 100Ω
- R40: value 10kΩ -> 1kΩ; footprint Resistor_SMD:R_0805_2012Metric -> Resistor_SMD:R_0603_1608Metric
- R41: value 330Ω -> 1kΩ
- R42: value 1kΩ -> 10kΩ; footprint Resistor_SMD:R_0603_1608Metric -> Resistor_SMD:R_0805_2012Metric
- R43: value 100kΩ -> 330Ω
- R44: value 2.7kΩ -> 1kΩ
- R45: value 140kΩ -> 100kΩ
- R46: value 10kΩ -> 2.7kΩ
- R47: value 100kΩ -> 140kΩ
- R48: value 47Ω -> 10kΩ
- R49: value 100mΩ -> 100kΩ; footprint Resistor_SMD:R_1206_3216Metric -> Resistor_SMD:R_0603_1608Metric
- R5: value 100mΩ -> 1kΩ; footprint Resistor_SMD:R_2010_5025Metric -> Resistor_SMD:R_0603_1608Metric
- R50: value 100mΩ -> 47Ω; footprint Resistor_SMD:R_1206_3216Metric -> Resistor_SMD:R_0603_1608Metric
- R51: value 31.2kΩ -> 100mΩ; footprint Resistor_SMD:R_0603_1608Metric -> Resistor_SMD:R_1206_3216Metric
- R52: value 10kΩ -> 100mΩ; footprint Resistor_SMD:R_0603_1608Metric -> Resistor_SMD:R_1206_3216Metric
- R53: value 3.92kΩ -> 31.2kΩ
- R54: value 750Ω -> 10kΩ
- R55: value 10kΩ -> 3.92kΩ
- R56: value 4.7kΩ -> 750Ω
- R57: value 4.7kΩ -> 10kΩ
- R58: value 10kΩ -> 4.7kΩ
- R59: value 100kΩ -> 4.7kΩ
- R60: value 100Ω -> 10kΩ
- R61: value 100Ω -> 100kΩ
- R62, R82: value 100kΩ -> 100Ω
- R64, R65, R66: value 47kΩ -> 100kΩ
- R67: value 10kΩ -> 47kΩ
- R68: value NI -> 47kΩ
- R69, R81: value 100kΩ -> 47kΩ
- R71, R72, R73: value 100Ω -> NI
- R74, R75, R78: footprint Resistor_SMD:R_0805_2012Metric -> Resistor_SMD:R_0603_1608Metric
- R76: value 0Ω -> NI; footprint Resistor_SMD:R_0805_2012Metric -> Resistor_SMD:R_0603_1608Metric
- R77: value NI -> 10kΩ; footprint Resistor_SMD:R_0805_2012Metric -> Resistor_SMD:R_0603_1608Metric
- R83, R84: value 20Ω -> 100Ω
- R85: value 100Ω -> 0Ω; footprint Resistor_SMD:R_0603_1608Metric -> Resistor_SMD:R_0805_2012Metric
- R86: value 100Ω -> NI; footprint Resistor_SMD:R_0603_1608Metric -> Resistor_SMD:R_0805_2012Metric
- R87: value 330Ω -> NI; footprint Resistor_SMD:R_0603_1608Metric -> Resistor_SMD:R_0805_2012Metric
- R88: value 330Ω -> 100kΩ
- R89, R91, R92: value 4.7kΩ -> 100kΩ
- R9: value 100mΩ -> 47RΩ; footprint Resistor_SMD:R_2010_5025Metric -> Resistor_SMD:R_0603_1608Metric
- R90: value 4.7kΩ -> 1kΩ
- R93, R94: value 1kΩ -> 20Ω
- R97, R98: value 2.2kΩ -> 330Ω
- U10: value 74HC245 -> 74HC2G32; footprint Package_SO:TSSOP-20_4.4x6.5mm_P0.65mm -> Package_SO:VSSOP-8_2.3x2mm_P0.5mm
- U11: value SHTC3 -> 74HC245; footprint footprints:DFN-4-1EP_2x2mm_P1mm_EP0.7x1.6mm -> Package_SO:TSSOP-20_4.4x6.5mm_P0.65mm
- U9: value 74HC2G32 -> MCP6002-xSN; footprint Package_SO:VSSOP-8_2.3x2mm_P0.5mm -> Package_SO:SOIC-8_3.9x4.9mm_P1.27mm
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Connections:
- C71 pad 1: INPUT3 -> Net-(C71-Pad1)
- C72 pad 2: Net-(C72-Pad2) -> GND
- C73 pad 1: EMERGENCY -> Net-(C73-Pad1)
- C74 pad 1: +5V -> Net-(C74-Pad1)
- C75 pad 1: KEY_3 -> INPUT3
- C76 pad 1: KEY_4 -> Net-(C76-Pad1)
- C76 pad 2: GND -> Net-(C76-Pad2)
- C77 pad 1: KEY_1 -> EMERGENCY
- C78 pad 1: KEY_2 -> +5V
- C79 pad 1: +3V3 -> KEY_3
- D19 pad 1: GND -> /Sockets/OPC1
- D19 pad 2: Net-(D19-Pad2) -> GND
- D23 pad 1: VS -> GND
- D24 pad 1: GND -> VS
- D25 pad 1: Net-(C51-Pad2) -> GND
- D25 pad 2: GND -> Net-(D25-Pad2)
- D26 pad 1: Net-(C51-Pad1) -> Net-(C51-Pad2)
- D26 pad 2: Net-(D26-Pad2) -> GND
- D27 pad 1: +12V -> Net-(C51-Pad1)
- D27 pad 2: Net-(D26-Pad2) -> Net-(D27-Pad2)
- D28 pad 1: Net-(C61-Pad2) -> +12V
- D28 pad 2: GND -> Net-(D27-Pad2)
- D29 pad 1: Net-(C59-Pad2) -> Net-(C61-Pad2)
- D29 pad 2: Net-(D29-Pad2) -> GND
- D30 pad 1: Net-(C61-Pad1) -> Net-(C59-Pad2)
- D30 pad 2: +3V3 -> Net-(D30-Pad2)
- D31 pad 1: Net-(D31-Pad1) -> Net-(C61-Pad1)
- D31 pad 2: GND -> +3V3
- D34 pad 1: Net-(D34-Pad1) -> VDDA
- D34 pad 2: GND -> Net-(C73-Pad1)
- D35 pad 1: Net-(D35-Pad1) -> Net-(C73-Pad1)
- D36 pad 1: Net-(D36-Pad1) -> VDDA
- D36 pad 2: GND -> Net-(C74-Pad1)
- D37 pad 1: Net-(D37-Pad1) -> Net-(C74-Pad1)
- D39 pad 1: VS -> Net-(D39-Pad1)
- D39 pad 2: Net-(D38-Pad1) -> GND
- D40 pad 1: +3V3 -> Net-(D40-Pad1)
- D40 pad 2: I2C_SCL -> GND
- D41 pad 1: I2C_SCL -> Net-(D41-Pad1)
- D42 pad 1: +3V3 -> 12V_PROTECTED
- D42 pad 2: I2C_SDA -> GND
- D43 pad 1: I2C_SDA -> Net-(D43-Pad1)
- D44 pad 1: Net-(D44-Pad1) -> VS
- D44 pad 2: GND -> Net-(D43-Pad1)
- D45 pad 1: Net-(D45-Pad1) -> +3V3
- D45 pad 2: GND -> I2C_SCL
- F1 pad 1: +5V -> Net-(D22-Pad2)
- F2 pad 1: +5V -> 24V_PROTECTED
- F2 pad 2: Net-(F2-Pad2) -> VS
- F3 pad 1: Net-(D21-Pad2) -> 12V_PROTECTED
- F3 pad 2: Net-(F3-Pad2) -> +12V
- F4 pad 1: VS -> +5V
- F4 pad 2: Net-(F4-Pad2) -> 5V_PROTECTED
- F5 pad 1: VS -> +3V3
- F5 pad 2: Net-(F5-Pad2) -> 3.3V_PROTECTED
- F6 pad 1: VS -> Net-(F6-Pad1)
- F6 pad 2: Net-(F6-Pad2) -> VS
- F7 pad 1: Net-(D37-Pad1) -> Net-(F7-Pad1)
- F7 pad 2: +12V -> +5V
- FB1 pad 1: Net-(C11-Pad2) -> +3V3
- FB1 pad 2: Net-(FB1-Pad2) -> +3V3
- FB10 pad 1: VDD -> VDDA
- FB2 pad 1: Net-(C13-Pad2) -> Net-(C11-Pad2)
- FB3 pad 1: Net-(C14-Pad1) -> Net-(C13-Pad2)
- FB4 pad 1: Net-(C12-Pad1) -> Net-(C14-Pad1)
- FB5 pad 1: Net-(C25-Pad2) -> Net-(C12-Pad1)
- FB6 pad 1: Net-(C27-Pad2) -> Net-(C25-Pad2)
- FB7 pad 1: Net-(C28-Pad1) -> Net-(C27-Pad2)
- FB8 pad 1: Net-(C26-Pad1) -> Net-(C28-Pad1)
- FB9 pad 1: VDDA -> Net-(C26-Pad1)
- FB9 pad 2: +3V3 -> Net-(FB9-Pad2)
- J11 pad 1: /Sockets/APGHP -> /Sockets/OAPGHP
- J11 pad 2: /Sockets/APG -> /Sockets/OAPG
- J11 pad 9: /Sockets/PC1 -> /Sockets/OPC1
- J14 pad 1: Net-(F1-Pad2) -> 5V_PROTECTED
- J15 pad 1: Net-(F2-Pad2) -> 5V_PROTECTED
- J16 pad 1: Net-(F3-Pad2) -> Net-(F1-Pad2)
- J17 pad 1: VS -> 24V_PROTECTED
- J18 pad 1: +12V -> 12V_PROTECTED
- J19 pad 1: +5V -> 5V_PROTECTED
- J20 pad 1: +3V3 -> 3.3V_PROTECTED
- J21 pad 1: Net-(F4-Pad2) -> 24V_PROTECTED
- J24 pad 1: Net-(F5-Pad2) -> 24V_PROTECTED
- J25 pad 1: Net-(F5-Pad2) -> 24V_PROTECTED
- J26 pad 1: Net-(F6-Pad2) -> Net-(J26-Pad1)
- J26 pad 2: Net-(J26-Pad2) -> GND
- J26 pad 3: GND -> Net-(J26-Pad3)
- J27 pad 1: Net-(J27-Pad1) -> 24V_PROTECTED
- J27 pad 2: Net-(D34-Pad1) -> Net-(J27-Pad2)
- J28 pad 1: Net-(J28-Pad1) -> 5V_PROTECTED
- J28 pad 2: Net-(D35-Pad1) -> Net-(D39-Pad1)
- J29 pad 1: Net-(D36-Pad1) -> 5V_PROTECTED
- J29 pad 2: Net-(D37-Pad1) -> Net-(D40-Pad1)
- J30 pad 1: Net-(F8-Pad1) -> Net-(D41-Pad1)
- J30 pad 2: Net-(D38-Pad1) -> 12V_PROTECTED
- J31 pad 1: Net-(J31-Pad1) -> Net-(F6-Pad1)
- J31 pad 2: Net-(C72-Pad2) -> Net-(D43-Pad1)
- J32 pad 2: Net-(C72-Pad2) -> Net-(C76-Pad2)
- J32 pad 3: Net-(J32-Pad3) -> Net-(C76-Pad1)
- J33 pad 1: Net-(F9-Pad2) -> Net-(J33-Pad1)
- J33 pad 2: Net-(J33-Pad2) -> Net-(C76-Pad2)
- J34 pad 1: Net-(F10-Pad2) -> Net-(F7-Pad1)
- J34 pad 2: SPI_MOSI_BUF -> Net-(J34-Pad2)
- J34 pad 3: SPI_SCLK_BUF -> Net-(J34-Pad3)
- J34 pad 4: /HMI/MISO -> Net-(J34-Pad4)
- J34 pad 5: GND -> Net-(J34-Pad5)
- J35 pad 1: Net-(F11-Pad2) -> Net-(F7-Pad1)
- J35 pad 2: Net-(J35-Pad2) -> SPI_MOSI_BUF
- J35 pad 3: GND -> SPI_SCLK_BUF
- J35 pad 4: Net-(J35-Pad4) -> /HMI/MISO
- J36 pad 1: Net-(J36-Pad1) -> 3.3V_PROTECTED
- J36 pad 2: Net-(D44-Pad1) -> Net-(J36-Pad2)
- J37 pad 2: Net-(D45-Pad1) -> Net-(D49-Pad1)
- J38 pad 2: GND -> Net-(D50-Pad1)
- K1 pad 1: Net-(D38-Pad1) -> Net-(D43-Pad1)
- K1 pad 4: Net-(J31-Pad1) -> Net-(J32-Pad1)
- K1 pad 8: Net-(J32-Pad1) -> Net-(J33-Pad1)
- K1 pad 9: Net-(J32-Pad3) -> Net-(J33-Pad3)
- Q1 pad 3: Net-(Q1-Pad3) -> LIMIT_Y_BACK
- Q11 pad 1: Net-(D31-Pad1) -> Net-(D32-Pad1)
- Q12 pad 1: Net-(D32-Pad1) -> Net-(D33-Pad1)
- Q13 pad 1: Net-(D33-Pad1) -> Net-(D38-Pad1)
- Q14 pad 3: Net-(D34-Pad1) -> Net-(D39-Pad1)
- Q15 pad 3: Net-(D35-Pad1) -> Net-(D40-Pad1)
- Q16 pad 3: Net-(D36-Pad1) -> Net-(D41-Pad1)
- Q18 pad 3: Net-(D45-Pad1) -> Net-(D50-Pad1)
- Q19 pad 3: Net-(D44-Pad1) -> Net-(D49-Pad1)
- Q2 pad 3: LIMIT_Y_BACK -> LIMIT_Y_FRONT
- Q3 pad 3: LIMIT_Y_FRONT -> LIMIT_Z_UP
- Q4 pad 3: LIMIT_Z_UP -> LIMIT_Z_DOWN
- Q5 pad 3: LIMIT_Z_DOWN -> /Sockets/OPE
- Q6 pad 3: /Sockets/OPE -> PRINTER_POWER_DETECT
- Q7 pad 3: PRINTER_POWER_DETECT -> /Sockets/OPC1
- Q8 pad 4: Net-(D23-Pad2) -> Net-(D24-Pad2)
- Q8 pad 5: Net-(D21-Pad2) -> Net-(D22-Pad2)
- Q8 pad 6: Net-(D21-Pad2) -> Net-(D22-Pad2)
- Q8 pad 7: Net-(D21-Pad2) -> Net-(D22-Pad2)
- Q8 pad 8: Net-(D21-Pad2) -> Net-(D22-Pad2)
- R1 pad 1: +3V3 -> UART_TX
- R1 pad 2: +3V3 -> UART_RX
- R10 pad 1: +5V -> VDD
- R10 pad 2: Net-(Q1-Pad1) -> NRST
- R11 pad 1: Net-(Q1-Pad3) -> Net-(R11-Pad1)
- R11 pad 2: +3V3 -> GND
- R12 pad 1: VDDA -> Net-(R12-Pad1)
- R12 pad 2: Net-(C31-Pad1) -> GND
- R13 pad 1: VDD -> Net-(J4-Pad1)
- R13 pad 2: NRST -> VDD
- R14 pad 1: Net-(R14-Pad1) -> +3V3
- R14 pad 2: GND -> Net-(D17-Pad2)
- R15 pad 1: Net-(R15-Pad1) -> Net-(J6-Pad1)
- R15 pad 2: GND -> +3V3
- R16 pad 1: Net-(J4-Pad1) -> Net-(J7-Pad1)
- R16 pad 2: VDD -> +3V3
- R17 pad 1: +3V3 -> Net-(J8-Pad1)
- R17 pad 2: Net-(D17-Pad2) -> +3V3
- R18 pad 1: Net-(J6-Pad1) -> Net-(J9-Pad1)
- R19 pad 1: Net-(J7-Pad1) -> Net-(J6-Pad1)
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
